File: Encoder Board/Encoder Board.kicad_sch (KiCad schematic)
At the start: 4 parts, among them J1 Conn_02x05_Odd_Even, J2 Conn_02x05_Odd_Even

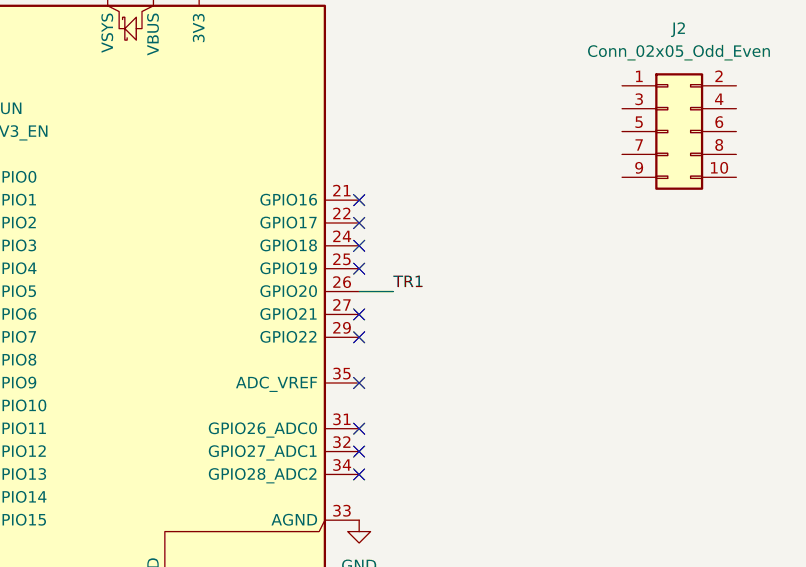
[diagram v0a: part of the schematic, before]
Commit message: testing latency with micropython native handlers
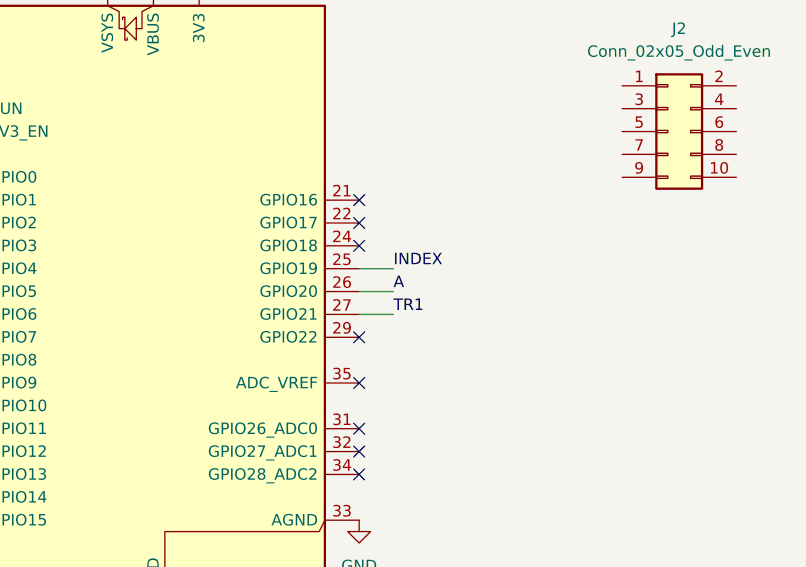
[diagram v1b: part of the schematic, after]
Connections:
- net TR1: now also A1.27 (GPIO21); no longer A1.26 (GPIO20)
- net INDEX: now reaches A1.25 (GPIO19)
- new net A: A1.26 (GPIO20)
- no-connect marks 28 -> 26
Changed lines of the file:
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@@
-	)
-	(no_connect
-		(at 134.62 63.5)
 	)
 	(no_connect
@@
 	(no_connect
 		(at 134.62 55.88)
-	)
-	(no_connect
-		(at 134.62 58.42)
 	)
 	(no_connect
@@
 	(wire
 		(pts
-			(xy 134.62 60.96) (xy 138.43 60.96)
+			(xy 134.62 63.5) (xy 138.43 63.5)
 		)
 		(stroke
@@
 	(wire
 		(pts
+			(xy 134.62 60.96) (xy 138.43 60.96)
+		)
+		(stroke
+			(width 0)
+			(type default)
+		)
+	)
+	(wire
+		(pts
 			(xy 106.68 25.4) (xy 106.68 22.86)
+		)
+		(stroke
+			(width 0)
+			(type default)
+		)
+	)
+	(wire
+		(pts
+			(xy 134.62 58.42) (xy 138.43 58.42)
 		)
 		(stroke
@@
 	)
 	(label "TR1"
+		(at 138.43 63.5 0)
+		(effects
+			(font
+				(size 1.27 1.27)
+			)
+			(justify left bottom)
+		)
+	)
+	(label "INDEX"
+		(at 138.43 58.42 0)
+		(effects
+			(font
+				(size 1.27 1.27)
+			)
+			(justify left bottom)
+		)
+	)
+	(label "A"
 		(at 138.43 60.96 0)
 		(effects

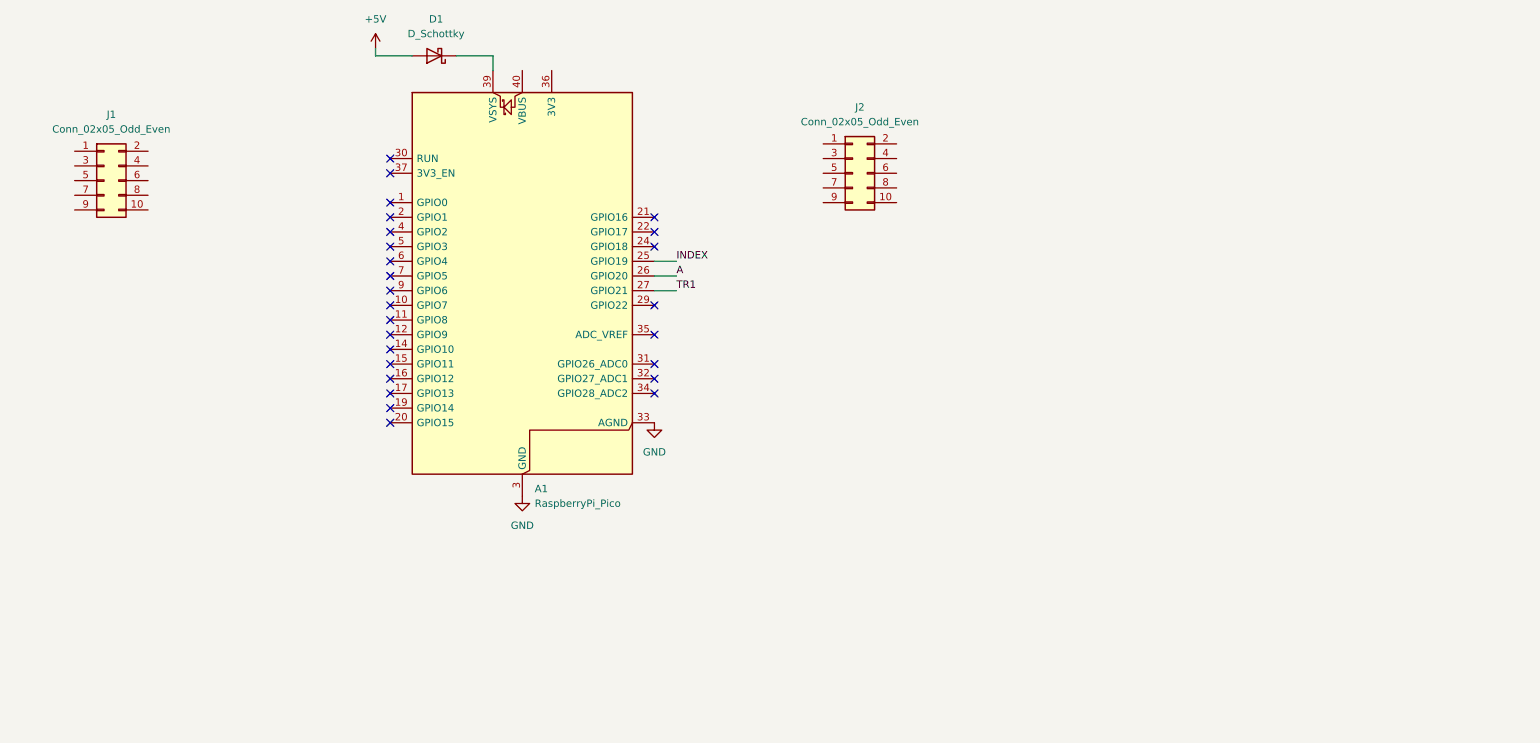
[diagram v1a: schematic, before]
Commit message: Schematic w/differential receiver and line driver
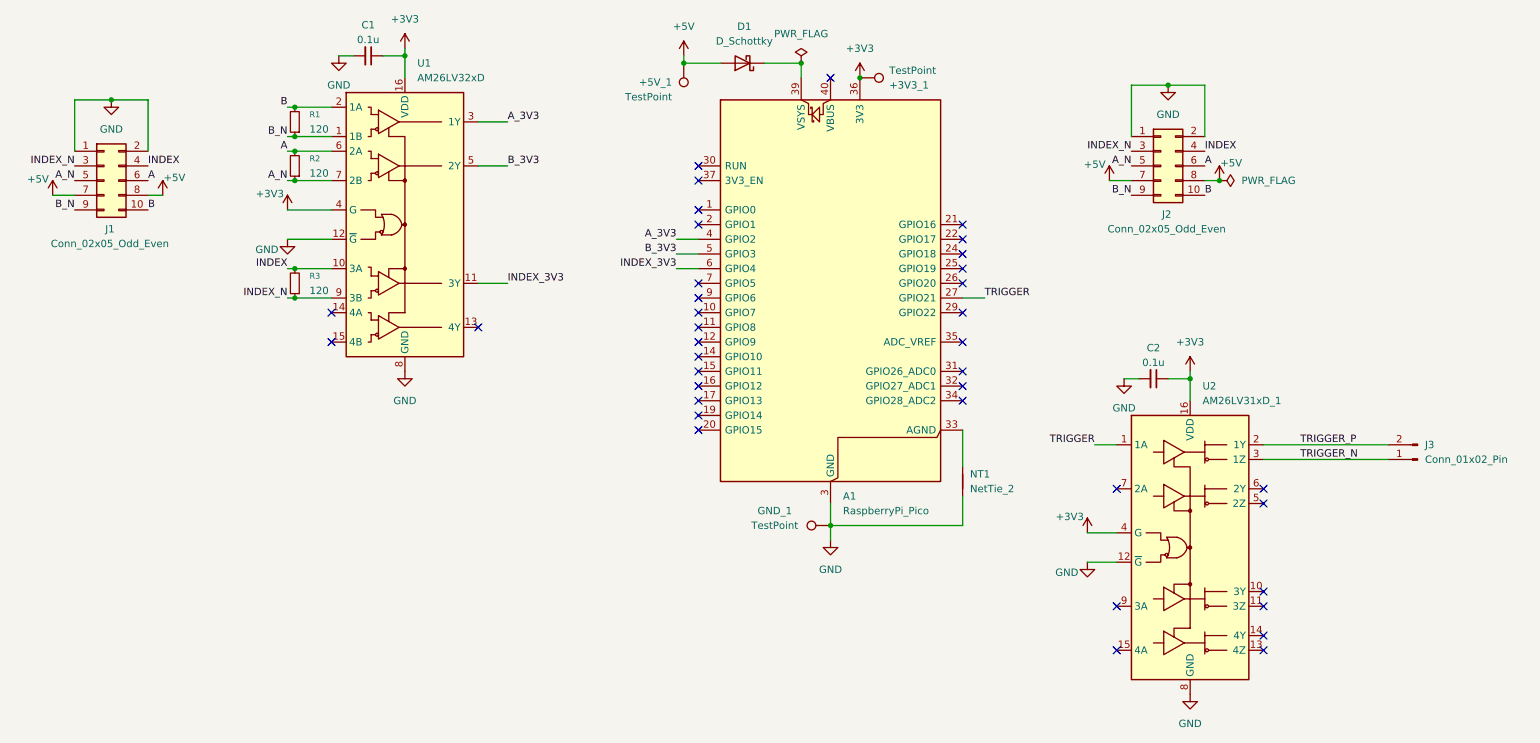
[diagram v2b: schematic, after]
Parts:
- added +3V3_1, +5V_1, GND_1: TestPoint, TestPoint:TestPoint_Pad_D2.0mm, symbol Connector:TestPoint
- added C1, C2: 0.1u, Capacitor_SMD:C_0805_2012Metric_Pad1.18x1.45mm_HandSolder, symbol Device:C_Small
- added J3: Conn_01x02_Pin, Connector_PinHeader_1.00mm:PinHeader_1x02_P1.00mm_Horizontal, symbol Connector:Conn_01x02_Pin
- added NT1: NetTie_2, NetTie:NetTie-2_SMD_Pad0.5mm, symbol Device:NetTie_2
- added R1, R2, R3: 120, Resistor_SMD:R_0805_2012Metric_Pad1.20x1.40mm_HandSolder, symbol Device:R_Small
- added U1: AM26LV32xD, Package_SO:SOIC-16_3.9x9.9mm_P1.27mm, symbol Interface:AM26LV32xD
- added U2: AM26LV31xD_1, Package_SO:SOIC-16_3.9x9.9mm_P1.27mm, symbol Interface:AM26LV31xD_1
- D1: footprint (none) -> Diode_SMD:D_SMA_Handsoldering
- J1, J2: footprint (none) -> Connector_Molex_Milligrid:Molex_8783210xx_2x05_P2.0mm_Header_Vertical
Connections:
- net +5V: now also J1.7 (Pin_7), J1.8 (Pin_8), J2.7 (Pin_7), J2.8 (Pin_8), +5V_1.1
- net A: now also J1.6 (Pin_6), J2.6 (Pin_6), R2.2, U1.6 (2A); no longer A1.26 (GPIO20)
- net GND: now also J1.1 (Pin_1), J1.2 (Pin_2), J2.1 (Pin_1), J2.2 (Pin_2), C1.2, C2.2, GND_1.1, NT1.1, U1.12 (~{G}), U1.8 (GND), U2.12 (~{G}), U2.8 (GND); no longer A1.33 (AGND)
- net INDEX: now also J1.4 (Pin_4), J2.4 (Pin_4), R3.2, U1.10 (3A); no longer A1.25 (GPIO19)
- net B: now reaches J2.10 (Pin_10)
- net B: now also J1.10 (Pin_10), R1.2, U1.2 (1A)
- net INDEX_N: now reaches J2.3 (Pin_3)
- net INDEX_N: now also J1.3 (Pin_3), R3.1, U1.9 (3B)
- net A_N: now reaches J2.5 (Pin_5)
- net A_N: now also J1.5 (Pin_5), R2.1, U1.7 (2B)
- net B_N: now reaches J2.9 (Pin_9)
- net B_N: now also J1.9 (Pin_9), R1.1, U1.1 (1B)
- net +3V3: now reaches A1.36 (3V3)
- net +3V3: now also +3V3_1.1, C1.1, C2.1, U1.16 (VDD), U1.4 (G), U2.16 (VDD), U2.4 (G)
- net A_3V3: now reaches A1.4 (GPIO2)
- net A_3V3: now also U1.3 (1Y)
- net B_3V3: now reaches A1.5 (GPIO3)
- net B_3V3: now also U1.5 (2Y)
- net INDEX_3V3: now reaches A1.6 (GPIO4)
- net INDEX_3V3: now also U1.11 (3Y)
- net TR1 renamed TRIGGER
- net TRIGGER: now also U2.1 (1A)
- new net: A1.33 (AGND), NT1.2
- new net TRIGGER_N: J3.1 (Pin_1), U2.3 (1Z)
- new net TRIGGER_P: J3.2 (Pin_2), U2.2 (1Y)
- no-connect marks 26 -> 38
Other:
- moved on the sheet: A1, D1

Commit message: Layout
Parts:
- J3: footprint Connector_PinHeader_1.00mm:PinHeader_1x02_P1.00mm_Horizontal -> Connector_PinHeader_2.00mm:PinHeader_1x02_P2.00mm_Vertical
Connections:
- net A: now also R1.2, U1.2 (1A); no longer R2.2, U1.6 (2A)
- net A_N: now also R1.1, U1.1 (1B); no longer R2.1, U1.7 (2B)
- net B: now also R2.2, U1.6 (2A); no longer R1.2, U1.2 (1A)
- net B_N: now also R2.1, U1.7 (2B); no longer R1.1, U1.1 (1B)
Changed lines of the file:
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@@
-		)
-	)
-	(label "B"
-		(at 71.12 31.75 180)
-		(effects
-			(font
-				(size 1.27 1.27)
-			)
-			(justify right bottom)
 		)
 	)
@@
 		)
 	)
+	(label "B_N"
+		(at 71.12 44.45 180)
+		(effects
+			(font
+				(size 1.27 1.27)
+			)
+			(justify right bottom)
+		)
+	)
 	(label "TRIGGER"
 		(at 191.77 64.77 0)
@@
 		)
 	)
-	(label "A"
-		(at 71.12 39.37 180)
-		(effects
-			(font
-				(size 1.27 1.27)
-			)
-			(justify right bottom)
-		)
-	)
 	(label "TRIGGER"
 		(at 210.82 90.17 180)
@@
 		)
 	)
+	(label "A_N"
+		(at 71.12 36.83 180)
+		(effects
+			(font
+				(size 1.27 1.27)
+			)
+			(justify right bottom)
+		)
+	)
 	(label "B"
 		(at 229.87 46.99 0)
@@
 		)
 	)
+	(label "A"
+		(at 71.12 31.75 180)
+		(effects
+			(font
+				(size 1.27 1.27)
+			)
+			(justify right bottom)
+		)
+	)
 	(label "B"
 		(at 46.99 49.53 0)
@@
 		)
 	)
-	(label "A_N"
-		(at 71.12 44.45 180)
-		(effects
-			(font
-				(size 1.27 1.27)
-			)
-			(justify right bottom)
-		)
-	)
 	(label "B_3V3"
 		(at 109.22 41.91 0)
@@
 		)
 	)
+	(label "B"
+		(at 71.12 39.37 180)
+		(effects
+			(font
+				(size 1.27 1.27)
+			)
+			(justify right bottom)
+		)
+	)
 	(label "B_N"
 		(at 34.29 49.53 180)
@@
 		)
 	)
-	(label "B_N"
-		(at 71.12 36.83 180)
-		(effects
-			(font
-				(size 1.27 1.27)
-			)
-			(justify right bottom)
-		)
-	)
 	(symbol
 		(lib_id "Interface:AM26LV32xD")
@@
 			)
 		)
-		(property "Footprint" "Connector_PinHeader_1.00mm:PinHeader_1x02_P1.00mm_Horizontal"
+		(property "Footprint" "Connector_PinHeader_2.00mm:PinHeader_1x02_P2.00mm_Vertical"
 			(at 266.7 92.71 0)
 			(hide yes)

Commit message: Update 2x5 connector footprint
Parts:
- J1, J2: footprint Connector_Molex_Milligrid:Molex_8783210xx_2x05_P2.0mm_Header_Vertical -> Connector_PinHeader_2.54mm:PinHeader_2x05_P2.54mm_Vertical
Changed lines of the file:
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@@
 			)
 		)
-		(property "Footprint" "Connector_Molex_Milligrid:Molex_8783210xx_2x05_P2.0mm_Header_Vertical"
+		(property "Footprint" "Connector_PinHeader_2.54mm:PinHeader_2x05_P2.54mm_Vertical"
 			(at 39.37 44.45 0)
 			(hide yes)
@@
 			)
 		)
-		(property "Footprint" "Connector_Molex_Milligrid:Molex_8783210xx_2x05_P2.0mm_Header_Vertical"
+		(property "Footprint" "Connector_PinHeader_2.54mm:PinHeader_2x05_P2.54mm_Vertical"
 			(at 222.25 41.91 0)
 			(hide yes)

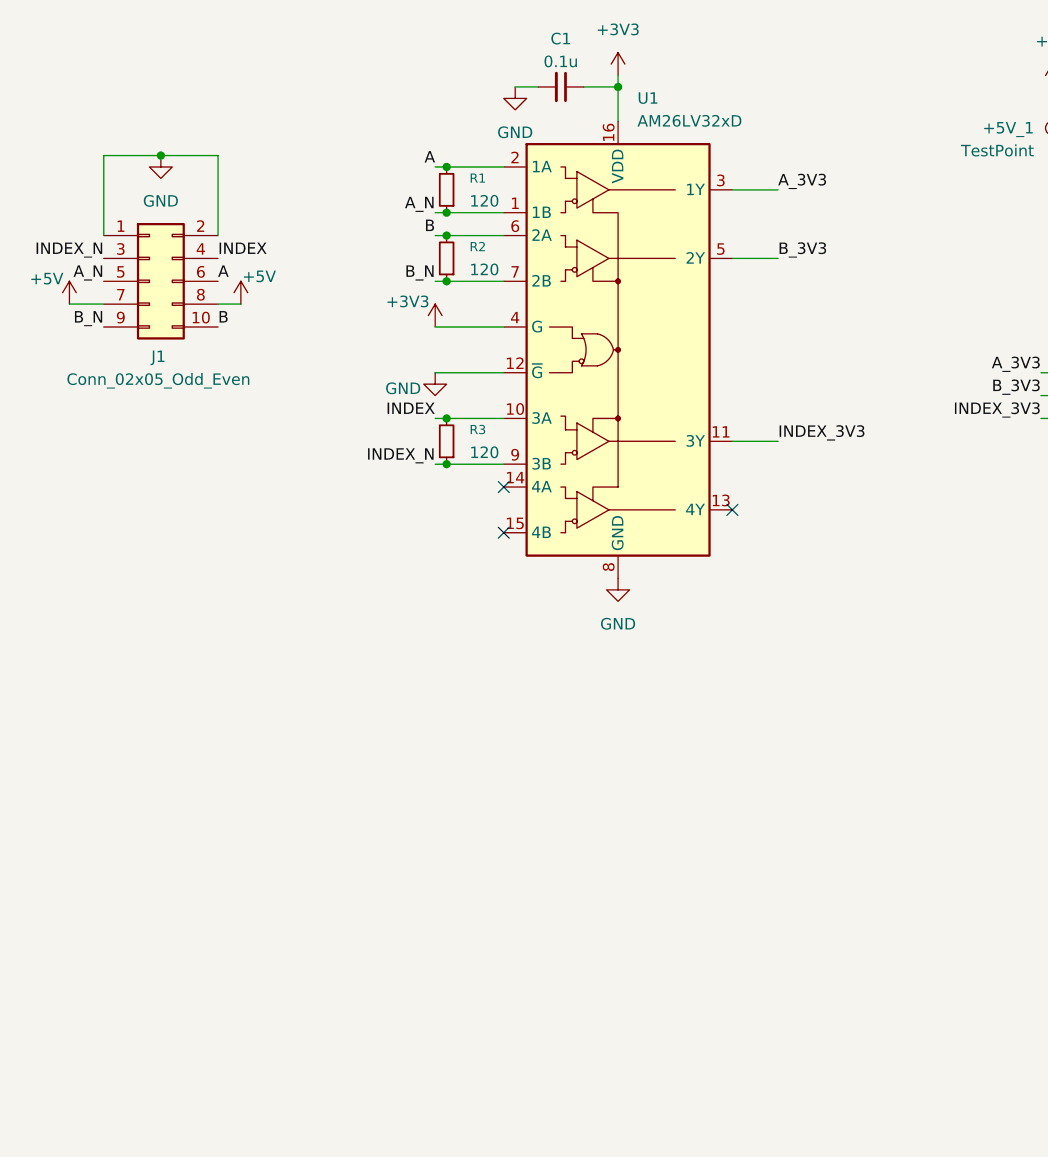
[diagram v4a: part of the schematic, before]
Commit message: Update diff pair terminating passives
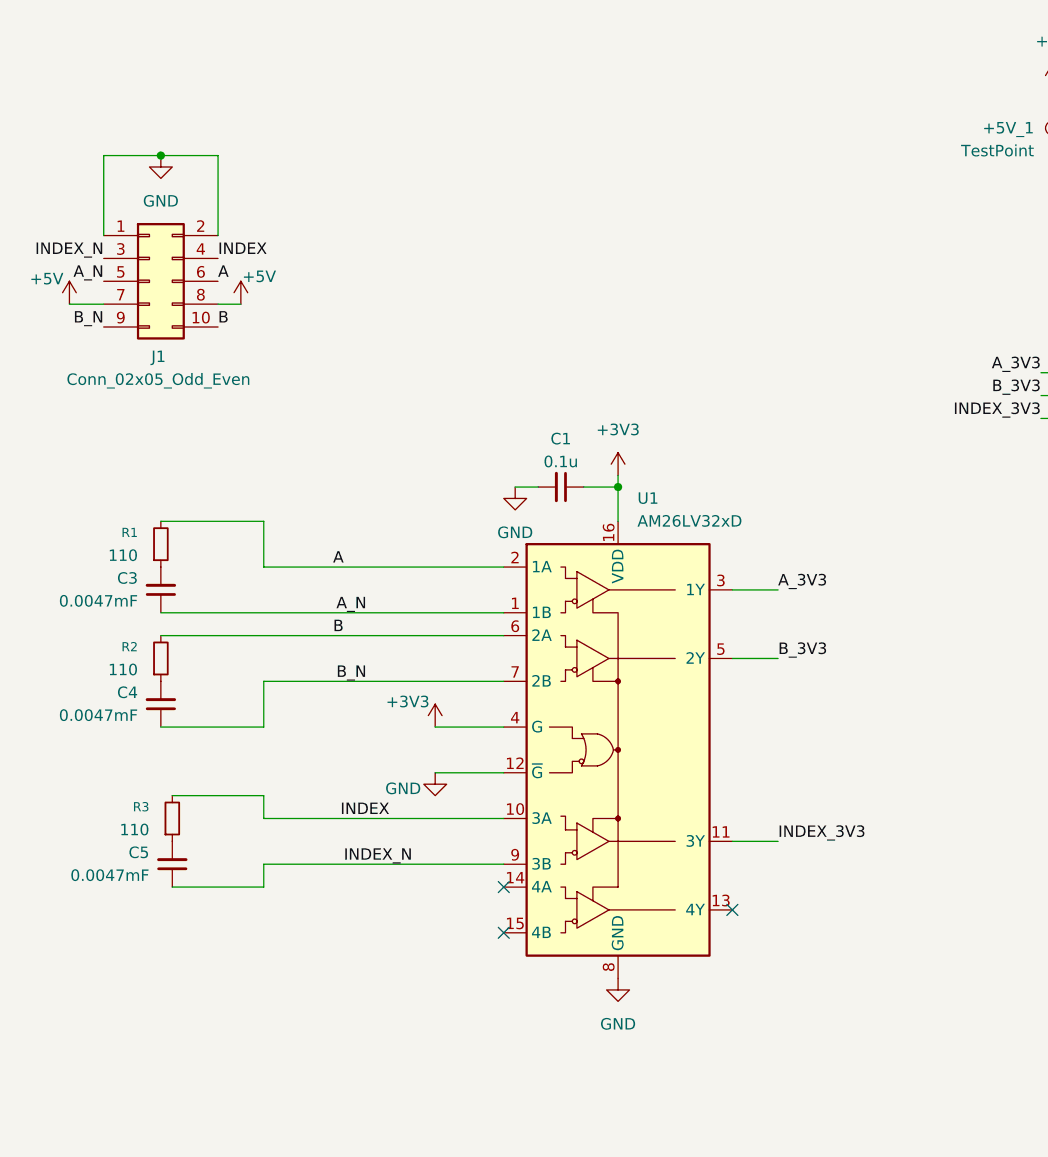
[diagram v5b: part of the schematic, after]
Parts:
- added C3, C4, C5: 0.0047mF, symbol Device:C_Small
- R1, R2, R3: value 120 -> 110
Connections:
- net A_N: now also C3.1; no longer R1.1
- net B_N: now also C4.1; no longer R2.1
- net INDEX_N: now also C5.1; no longer R3.1
- new net: C3.2, R1.1
- new net: C4.2, R2.1
- new net: C5.2, R3.1
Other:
- moved on the sheet: C1, U1

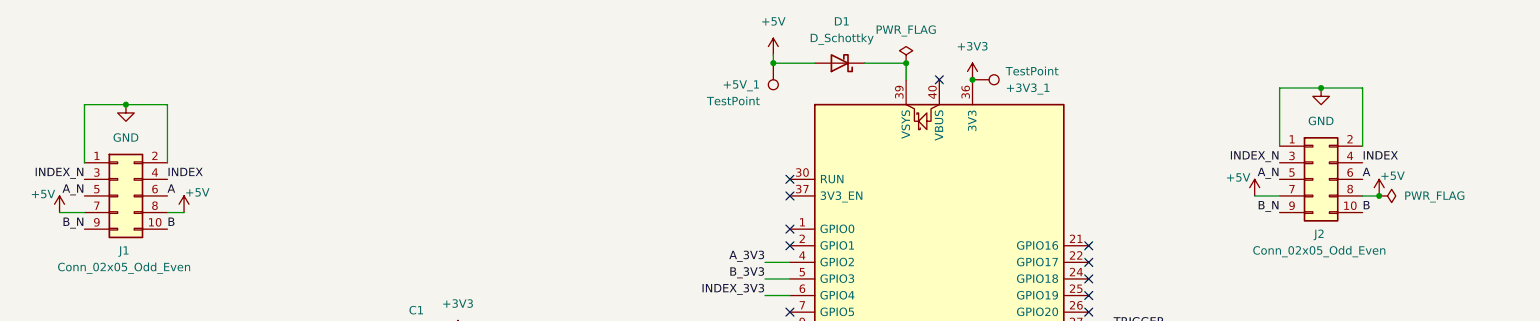
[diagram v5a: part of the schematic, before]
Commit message: Update layout with new passives
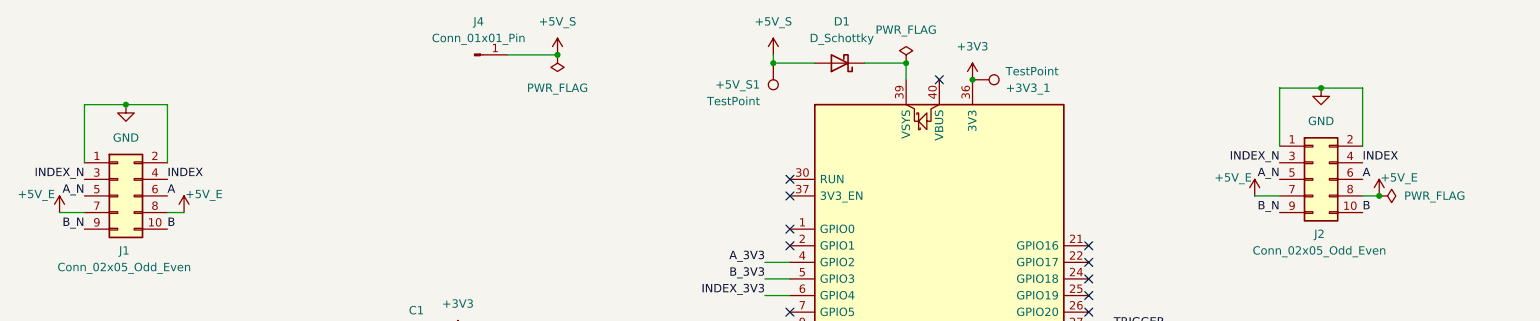
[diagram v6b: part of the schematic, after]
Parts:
- added J4: Conn_01x01_Pin, Connector_PinHeader_2.54mm:PinHeader_1x01_P2.54mm_Vertical, symbol Connector:Conn_01x01_Pin
- C3, C4, C5: footprint (none) -> Capacitor_SMD:C_0805_2012Metric_Pad1.18x1.45mm_HandSolder
- renumbered +5V_1 to +5V_S1
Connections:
- net +5V renamed +5V_E
- net +5V_E: no longer +5V_S1.1, D1.2 (A)
- new net +5V_S: +5V_S1.1, D1.2 (A), J4.1 (Pin_1)
